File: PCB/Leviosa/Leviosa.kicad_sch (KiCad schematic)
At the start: 50 parts, among them J3 Conn_01x03, Q3 TIP122, Q4 TIP122, U1 LM324, U2 ATtiny13A-P, U3 TPS1H200AQDGNRQ1, U5 L7805, U6 SS495A

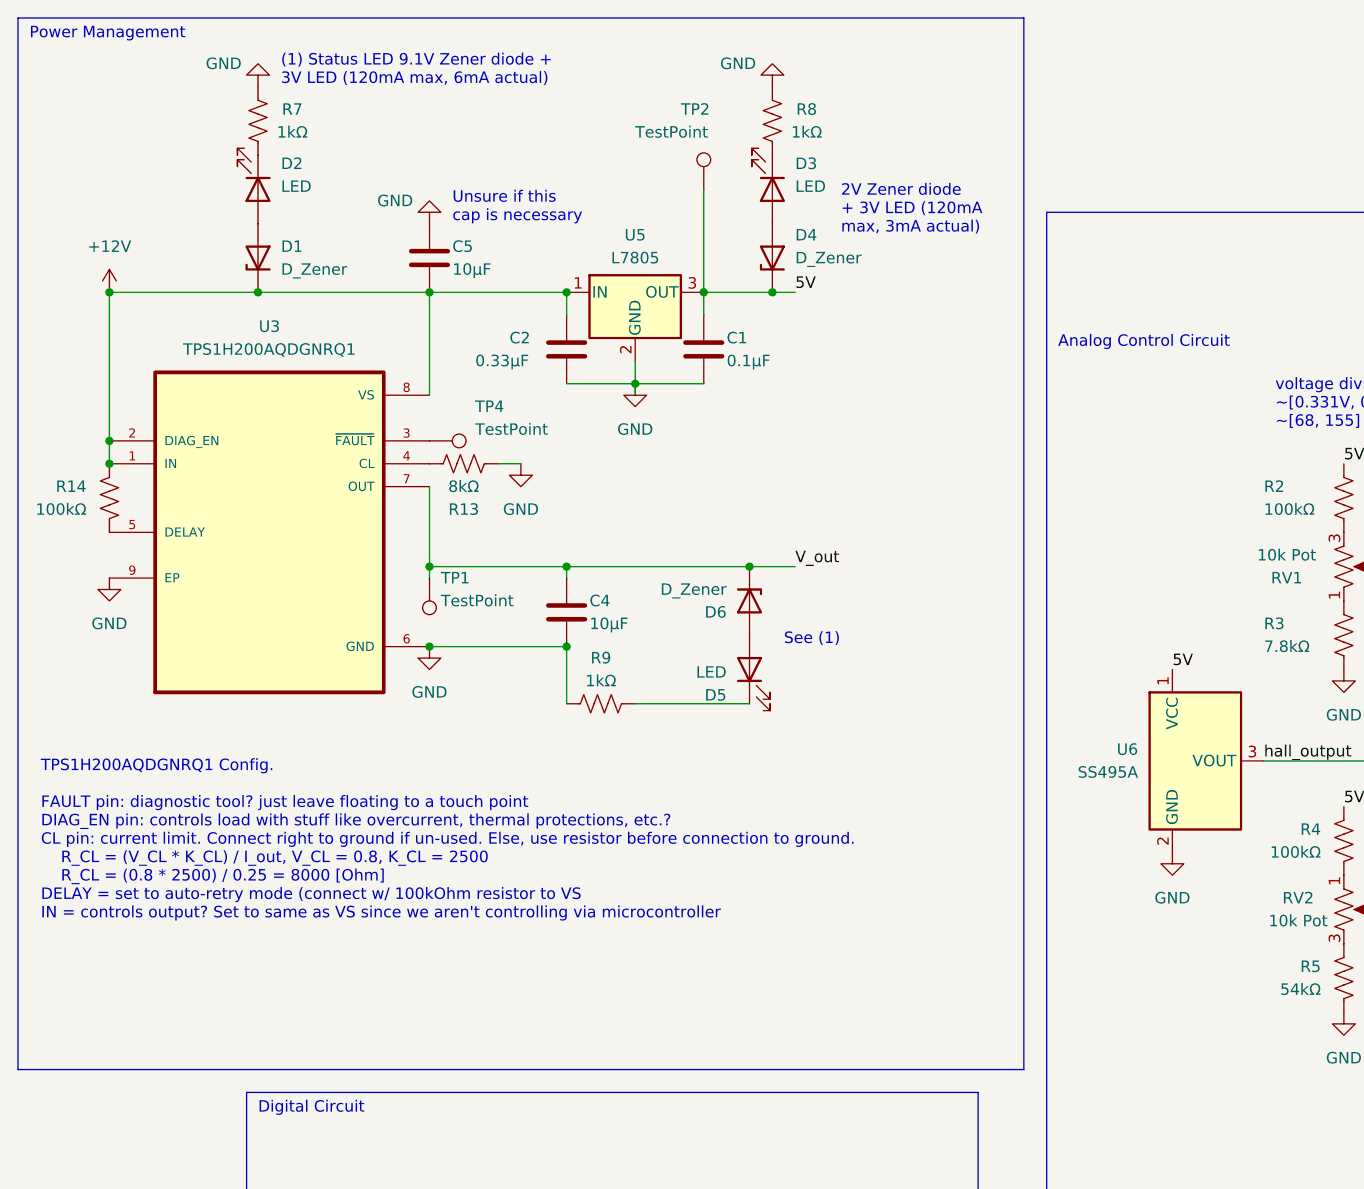
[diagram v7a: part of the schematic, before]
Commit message: update footprints and the like
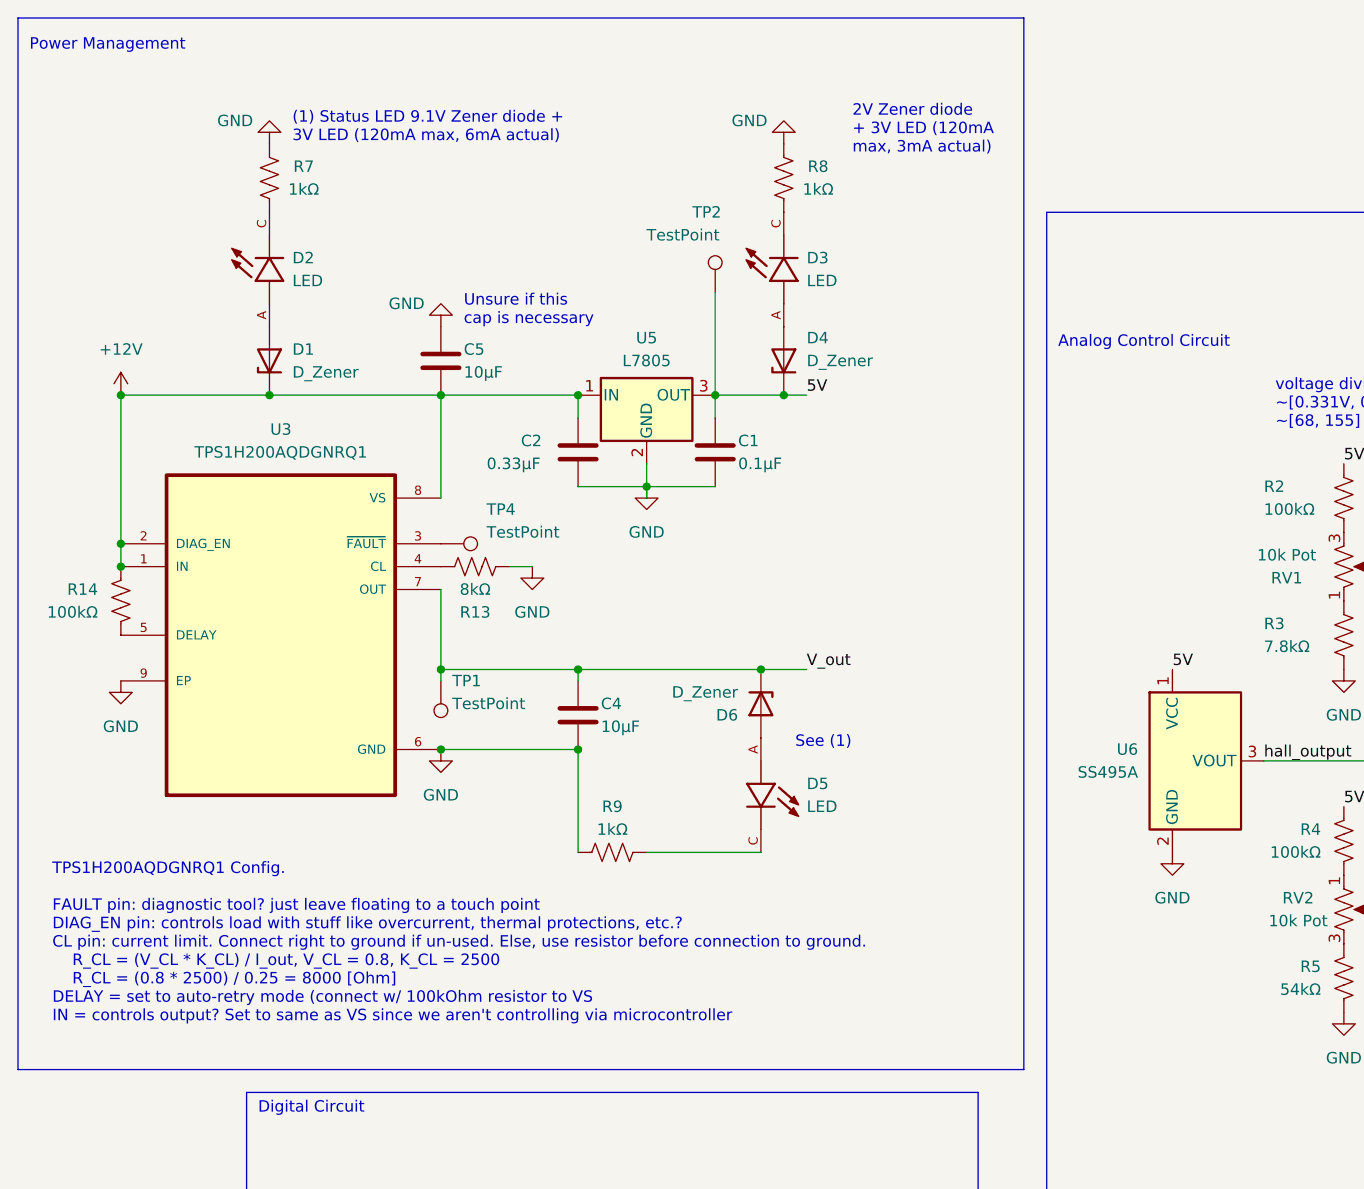
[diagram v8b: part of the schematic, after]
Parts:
- removed D2, D3, D5: LED, MP-2016-1100-50-70:LED_MP-2016-1100-50-70, symbol Device:LED
- added D2, D3, D5: LED, MP-2016-1100-50-70:LED_MP-2016-1100-50-70, symbol MP-2016-1100-50-70:MP-2016-1100-50-70
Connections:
- net at D6.2 (A): now also D5.A
- net at R7.1: now also D2.C
- net at R9.1: now also D5.C
- net at D4.2 (A): now also D3.A
- net at R8.1: now also D3.C
- net at D1.2 (A): now also D2.A
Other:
- moved on the sheet: C1, C2, C4, C5, D1, D4, D6, R13, R14, R7, R8, R9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
